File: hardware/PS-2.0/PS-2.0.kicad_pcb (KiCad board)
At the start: 2 copper layers, 119.7 x 199.4 mm, 51 parts, among them J1 PinSocket_02x16_P2.54mm_Verti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, J2 Conn_01x05, J3 Conn_01x05, J8 Conn_01x03, J9 Conn_01x03, K1 RAYEX-L90, K2 RAYEX-L90, Q1 IRFPE50, Q2 IRFPE50, Q3 IRFPE50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

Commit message: modified:   .DS_Store 	modified:   README.md 	deleted:    hardware/MSD-1.0/MSD-1.0 BoM.csv 	deleted:    hardware/MSD-1.0/MSD-1.0-backups/MSD-1.0-2025-04-08_110759.zip 	deleted:    hardware/MSD-1.0/MSD-1.0-backups/MSD-1.0-2025-04-08_111313.zip 	new file:   hardware/MSD-1.0/MSD-1.0-backups/MSD-1.0-2025-05-06_093009.zip 	new file:   hardware/MSD-1.0/MSD-1.0-backups/MSD-1.0-2025-05-06_093605.zip 	modified:   hardware/MSD-1.0/MSD-1.0.kicad_pcb 	modified:   hardware/MSD-1.0/MSD-1.0.kicad_sch 	modified:   hardware/MSD-1.0/fp-info-cache 	deleted:    hardware/PS-1.0/PS-1.0-backups/PS-1.0-2025-04-16_161300.zip 	deleted:    hardware/PS-1.0/PS-1.0-backups/PS-1.0-2025-04-16_162332.zip 	deleted:    hardware/PS-1.0/PS-1.0-backups/PS-1.0-2025-04-16_163259.zip 	deleted:    hardware/PS-1.0/PS-1.0-backups/PS-1.0-2025-04-17_110908.zip 	deleted:    hardware/PS-1.0/PS-1.0-backups/PS-1.0-2025-04-17_114838.zip 	deleted:    hardware/PS-1.0/PS-1.0-backups/PS-1.0-2025-04-17_155117.zip 	new file:   hardware/PS-1.0/PS-1.0-backups/PS-1.0-2025-05-06_094214.zip 	new file:   hardware/PS-1.0/PS-1.0-backups/PS-1.0-2025-05-06_095559.zip 	new file:   hardware/PS-1.0/PS-1.0-backups/PS-1.0-2025-05-06_100430.zip 	new file:   hardware/PS-1.0/PS-1.0-backups/PS-1.0-2025-05-06_100931.zip 	new file:   hardware/PS-1.0/PS-1.0-backups/PS-1.0-2025-05-06_101736.zip 	new file:   hardware/PS-1.0/PS-1.0-backups/PS-1.0-2025-05-06_102708.zip 	modified:   hardware/PS-1.0/PS-1.0.kicad_pcb 	modified:   hardware/PS-1.0/PS-1.0.kicad_sch 	new file:   hardware/PS-2.0/PS-2.0-B_Cu.gbr 	new file:   hardware/PS-2.0/PS-2.0-B_Mask.gbr 	new file:   hardware/PS-2.0/PS-2.0-B_Paste.gbr 	new file:   hardware/PS-2.0/PS-2.0-B_Silkscreen.gbr 	new file:   hardware/PS-2.0/PS-2.0-Edge_Cuts.gbr 	new file:   hardware/PS-2.0/PS-2.0-F_Cu.gbr 	new file:   hardware/PS-2.0/PS-2.0-F_Mask.gbr 	new file:   hardware/PS-2.0/PS-2.0-F_Paste.gbr 	new file:   hardware/PS-2.0/PS-2.0-F_Silkscreen.gbr 	new file:   hardware/PS-2.0/PS-2.0-NPTH.drl 	new file:   har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
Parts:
- moved D7 15.9 mm to (208.9, 196.8), turned to 0 degrees
- moved R5 13.3 mm to (229.2, 186.7), turned to 180 degrees
- moved L7 7.94 mm to (208.9, 191.8), turned to 0 degrees
- moved H1 5.72 mm to (216.2, 35.2)
- moved H2 5.72 mm to (216.2, 222.6)
- moved CON-01 3.51 mm to (232.9, 196.8)
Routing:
- net Net-(C4-Pad1): track 114.6 -> 186.0 mm
- net Net-(J1-Pin_9): track 85.7 -> 107.9 mm
- net Net-(J1-Pin_8): track 57.9 -> 77.3 mm
- net Net-(J1-Pin_7): track 61.7 -> 78.4 mm
- net Net-(J1-Pin_6): track 95.6 -> 110.5 mm
- net Net-(J1-Pin_5): track 98.4 -> 111.1 mm
- net /RLY-K: track 144.7 -> 155.2 mm
- net /RLY-A: track 124.0 -> 132.2 mm
- net /PWM: track 50.5 -> 54.7 mm
- added copper zone on B.Cu, net Net-(CON-01-Pin_2)
- added copper zone on B.Cu, net Net-(D7-K)
- added copper zone on B.Cu, net VS
- added copper zone on F.Cu, net VS

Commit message: modified:   .DS_Store 	modified:   README.md 	modified:   hardware/MSD-1.0/MSD-1.0-B_Cu.gbr 	modified:   hardware/MSD-1.0/MSD-1.0-B_Mask.gbr 	modified:   hardware/MSD-1.0/MSD-1.0-B_Paste.gbr 	modified:   hardware/MSD-1.0/MSD-1.0-B_Silkscreen.gbr 	modified:   hardware/MSD-1.0/MSD-1.0-Edge_Cuts.gbr 	modified:   hardware/MSD-1.0/MSD-1.0-F_Cu.gbr 	modified:   hardware/MSD-1.0/MSD-1.0-F_Mask.gbr 	modified:   hardware/MSD-1.0/MSD-1.0-F_Paste.gbr 	modified:   hardware/MSD-1.0/MSD-1.0-F_Silkscreen.gbr 	modified:   hardware/MSD-1.0/MSD-1.0-NPTH.drl 	modified:   hardware/MSD-1.0/MSD-1.0-PTH.drl 	deleted:    hardware/MSD-1.0/MSD-1.0-backups/MSD-1.0-2025-04-09_135836.zip 	deleted:    hardware/MSD-1.0/MSD-1.0-backups/MSD-1.0-2025-04-09_140350.zip 	new file:   hardware/MSD-1.0/MSD-1.0-backups/MSD-1.0-2025-05-08_171110.zip 	new file:   hardware/MSD-1.0/MSD-1.0-backups/MSD-1.0-2025-05-09_084805.zip 	modified:   hardware/MSD-1.0/MSD-1.0-job.gbrjob 	modified:   hardware/MSD-1.0/MSD-1.0.kicad_sch 	modified:   hardware/MSD-1.0/MSD-1.zip 	deleted:    hardware/MSD-1.0/~MSD-1.0.kicad_sch.lck 	modified:   hardware/PS-2.0/PS-2.0-B_Cu.gbr 	modified:   hardware/PS-2.0/PS-2.0-B_Mask.gbr 	modified:   hardware/PS-2.0/PS-2.0-B_Paste.gbr 	modified:   hardware/PS-2.0/PS-2.0-B_Silkscreen.gbr 	modified:   hardware/PS-2.0/PS-2.0-Edge_Cuts.gbr 	modified:   hardware/PS-2.0/PS-2.0-F_Cu.gbr 	modified:   hardware/PS-2.0/PS-2.0-F_Mask.gbr 	modified:   hardware/PS-2.0/PS-2.0-F_Paste.gbr 	modified:   hardware/PS-2.0/PS-2.0-F_Silkscreen.gbr 	modified:   hardware/PS-2.0/PS-2.0-NPTH.drl 	modified:   hardware/PS-2.0/PS-2.0-PTH.drl 	new file:   hardware/PS-2.0/PS-2.0-backups/PS-2.0-2025-05-09_084820.zip 	new file:   hardware/PS-2.0/PS-2.0-backups/PS-2.0-2025-05-09_090220.zip 	modified:   hardware/PS-2.0/PS-2.0-job.gbrjob 	modified:   hardware/PS-2.0/PS-2.0.kicad_pcb 	modified:   hardware/PS-2.0/PS-2.zip
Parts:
- removed HS3: Heatsink, Heatsink:Heatsink_Custom_10x18x50
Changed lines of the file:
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@@
 		)
 		(property "Value" "10A10"
-			(at 7.62 3.77 360)
+			(at 7.62 3.77 0)
 			(layer "F.Fab")
 			(effects
@@
 		)
 		(fp_text user "K"
-			(at 0 -2.3 360)
+			(at 0 -2.3 0)
 			(layer "F.Fab")
 			(effects
@@
 		)
 		(fp_text user "${REFERENCE}"
-			(at 8.295 0 360)
+			(at 8.295 0 0)
 			(layer "F.Fab")
 			(effects
@@
 		)
 		(property "Value" "L"
-			(at 7.62 3.12 360)
+			(at 7.62 3.12 0)
 			(layer "F.Fab")
 			(effects
@@
 		)
 		(fp_text user "${REFERENCE}"
-			(at 7.62 0 360)
+			(at 7.62 0 0)
 			(layer "F.Fab")
 			(effects
@@
 		)
 		(property "Value" "120Ω 2W"
-			(at 10.16 3.62 360)
+			(at 10.16 3.62 0)
 			(layer "F.Fab")
 			(effects
@@
 		)
 		(fp_text user "${REFERENCE}"
-			(at 10.16 0 360)
+			(at 10.16 0 0)
 			(layer "F.Fab")
 			(effects
@@
 			)
 			(scale
-				(xyz 1 1 1)
-			)
-			(rotate
-				(xyz 0 0 0)
-			)
-		)
-	)
-	(footprint "Heatsink:Heatsink_Custom_10x18x50"
-		(layer "F.Cu")
-		(at 230.8225 89.2175 -90)
-		(descr "Heatsink, StoneCold HS")
-		(tags "heatsink")
-		(property "Reference" "HS3"
-			(at 0 -8.85 90)
-			(layer "F.SilkS")
-			(hide yes)
-			(effects
-				(font
-					(size 1 1)
-					(thickness 0.15)
-				)
-			)
-		)
-		(property "Value" "Heatsink"
-			(at 0 -2.7 90)
-			(layer "F.Fab")
-			(hide yes)
-			(effects
-				(font
-					(size 1 1)
-					(thickness 0.15)
-				)
-			)
-		)
-		(property "Footprint" "Heatsink:Heatsink_Custom_10x18x50"
-			(at 0 -12.7 -90)
-			(unlocked yes)
-			(layer "F.Fab")
-			(hide yes)
-			(effects
-				(font
-					(size 1.27 1.27)
-					(thickness 0.15)
-				)
-			)
-		)
-		(property "Datasheet" ""
-			(at 0 -12.7 -90)
-			(unlocked yes)
-			(layer "F.Fab")
-			(hide yes)
-			(effects
-				(font
-					(size 1.27 1.27)
-					(thickness 0.15)
-				)
-			)
-		)
-		(property "Description" "Heatsink"
-			(at 0 -12.7 -90)
-			(unlocked yes)
-			(layer "F.Fab")
-			(hide yes)
-			(effects
-				(font
-					(size 1.27 1.27)
-					(thickness 0.15)
-				)
-			)
-		)
-		(property ki_fp_filters "Heatsink_*")
-		(sheetname "Root")
-		(sheetfile "PS-1.0.kicad_sch")
-		(attr through_hole)
-		(fp_line
-			(start -50 0)
-			(end -50 -18)
-			(stroke
-				(width 0.15)
-				(type default)
-			)
-			(layer "F.SilkS")
-		)
-		(fp_line
-			(start 50 0)
-			(end -50 0)
-			(stroke
-				(width 0.15)
-				(type default)
-			)
-			(layer "F.SilkS")
-		)
-		(fp_line
-			(start 50 0)
-			(end 50 -18)
-			(stroke
-				(width 0.15)
-				(type default)
-			)
-			(layer "F.SilkS")
-		)
-		(fp_line
-			(start 50 -18)
-			(end -50 -18)
-			(stroke
-				(width 0.15)
-				(type default)
-			)
-			(layer "F.SilkS")
-		)
-		(fp_line
-			(start -50 0)
-			(end -50 -18)
-			(stroke
-				(width 0.05)
-				(type default)
-			)
-			(layer "F.CrtYd")
-		)
-		(fp_line
-			(start 50 0)
-			(end -50 0)
-			(stroke
-				(width 0.05)
-				(type default)
-			)
-			(layer "F.CrtYd")
-		)
-		(fp_line
-			(start -50 -18)
-			(end 50 -18)
-			(stroke
-				(width 0.05)
-				(type default)
-			)
-			(layer "F.CrtYd")
-		)
-		(fp_line
-			(start 50 -18)
-			(end 50 0)
-			(stroke
-				(width 0.05)
-				(type default)
-			)
-			(layer "F.CrtYd")
-		)
-		(fp_text user "${REFERENCE}"
-			(at 0 -6.35 90)
-			(layer "F.Fab")
-			(effects
-				(font
-					(size 1 1)
-					(thickness 0.15)
-				)
-			)
-		)
-		(model "/Users/margabudi/Documents/ACAD/doc/Heatsink/10x18x50.step"
-			(offset
-				(xyz -50 0 0)
-			)
-			(scale

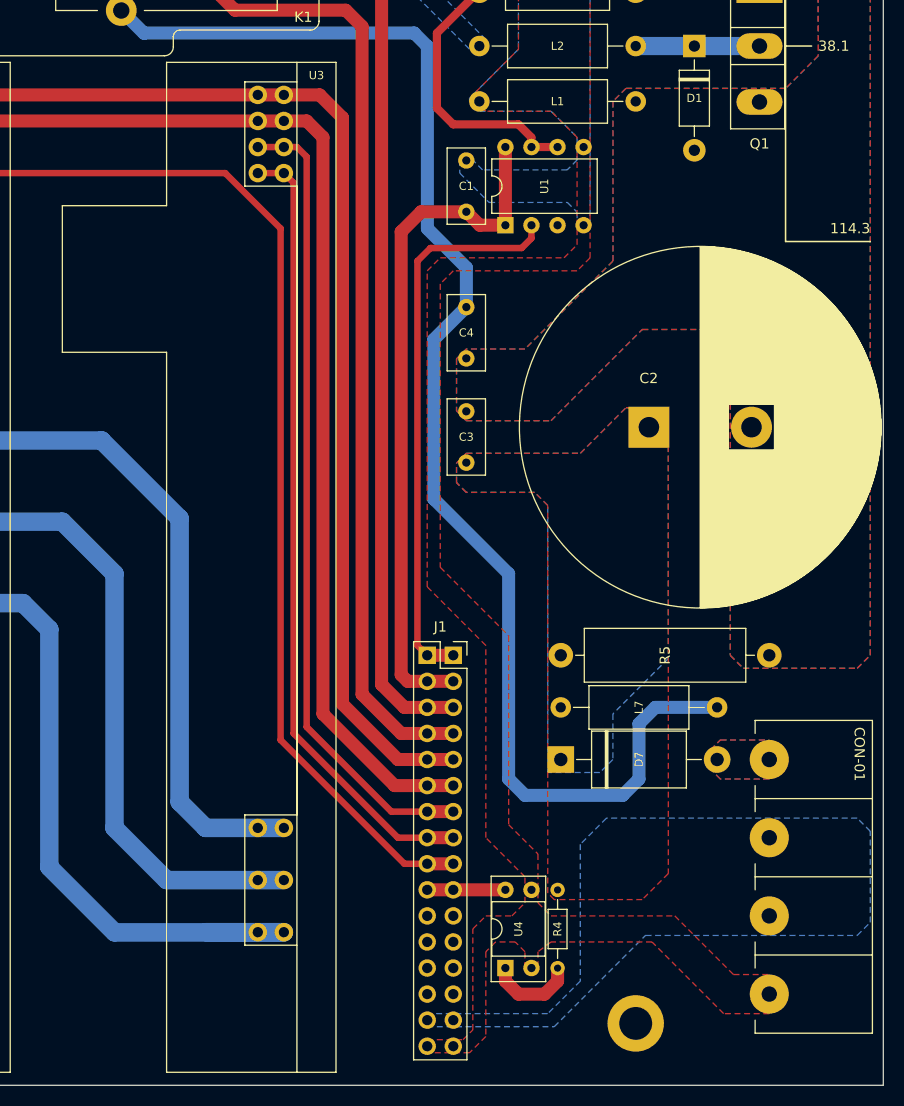
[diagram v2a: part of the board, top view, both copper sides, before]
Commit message: modified:   .DS_Store 	new file:   hardware/CTL-1.0/CTL-1.0-backups/CTL-1.0-2025-05-23_140814.zip 	new file:   hardware/CTL-1.0/CTL-1.0-backups/CTL-1.0-2025-05-23_142136.zip 	new file:   hardware/CTL-1.0/CTL-1.0-backups/CTL-1.0-2025-05-23_145207.zip 	new file:   hardware/CTL-1.0/CTL-1.0-backups/CTL-1.0-2025-05-23_145749.zip 	new file:   hardware/CTL-1.0/CTL-1.0-backups/CTL-1.0-2025-05-27_175205.zip 	new file:   hardware/CTL-1.0/CTL-1.0-backups/CTL-1.0-2025-05-27_180035.zip 	new file:   hardware/CTL-1.0/CTL-1.0-backups/CTL-1.0-2025-05-27_181441.zip 	new file:   hardware/CTL-1.0/CTL-1.0-backups/CTL-1.0-2025-05-27_182529.zip 	new file:   hardware/CTL-1.0/CTL-1.0-backups/CTL-1.0-2025-05-27_183819.zip 	new file:   hardware/CTL-1.0/CTL-1.0-backups/CTL-1.0-2025-05-28_201558.zip 	new file:   hardware/CTL-1.0/CTL-1.0-backups/CTL-1.0-2025-05-28_202523.zip 	new file:   hardware/CTL-1.0/CTL-1.0-backups/CTL-1.0-2025-05-28_203223.zip 	new file:   hardware/CTL-1.0/CTL-1.0-backups/CTL-1.0-2025-05-28_203806.zip 	new file:   hardware/CTL-1.0/CTL-1.0-backups/CTL-1.0-2025-05-28_204313.zip 	new file:   hardware/CTL-1.0/CTL-1.0-backups/CTL-1.0-2025-05-30_173028.zip 	new file:   hardware/CTL-1.0/CTL-1.0-backups/CTL-1.0-2025-05-30_174116.zip 	new file:   hardware/CTL-1.0/CTL-1.0-backups/CTL-1.0-2025-05-30_175122.zip 	new file:   hardware/CTL-1.0/CTL-1.0-backups/CTL-1.0-2025-05-30_180325.zip 	new file:   hardware/CTL-1.0/CTL-1.0-backups/CTL-1.0-2025-05-30_180909.zip 	new file:   hardware/CTL-1.0/CTL-1.0-backups/CTL-1.0-2025-06-03_185115.zip 	new file:   hardware/CTL-1.0/CTL-1.0-backups/CTL-1.0-2025-06-03_190157.zip 	new file:   hardware/CTL-1.0/CTL-1.0-backups/CTL-1.0-2025-06-03_222127.zip 	new file:   hardware/CTL-1.0/CTL-1.0-backups/CTL-1.0-2025-06-03_222647.zip 	new file:   hardware/CTL-1.0/CTL-1.0-backups/CTL-1.0-2025-06-03_223358.zip 	new file:   hardware/CTL-1.0/CTL-1.0-backups/CTL-1.0-2025-06-03_223905.zip 	modified:   hardware/CTL-1.0/CTL-1.0.kicad_pcb 	new file:   hardware/CTL-1.0/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
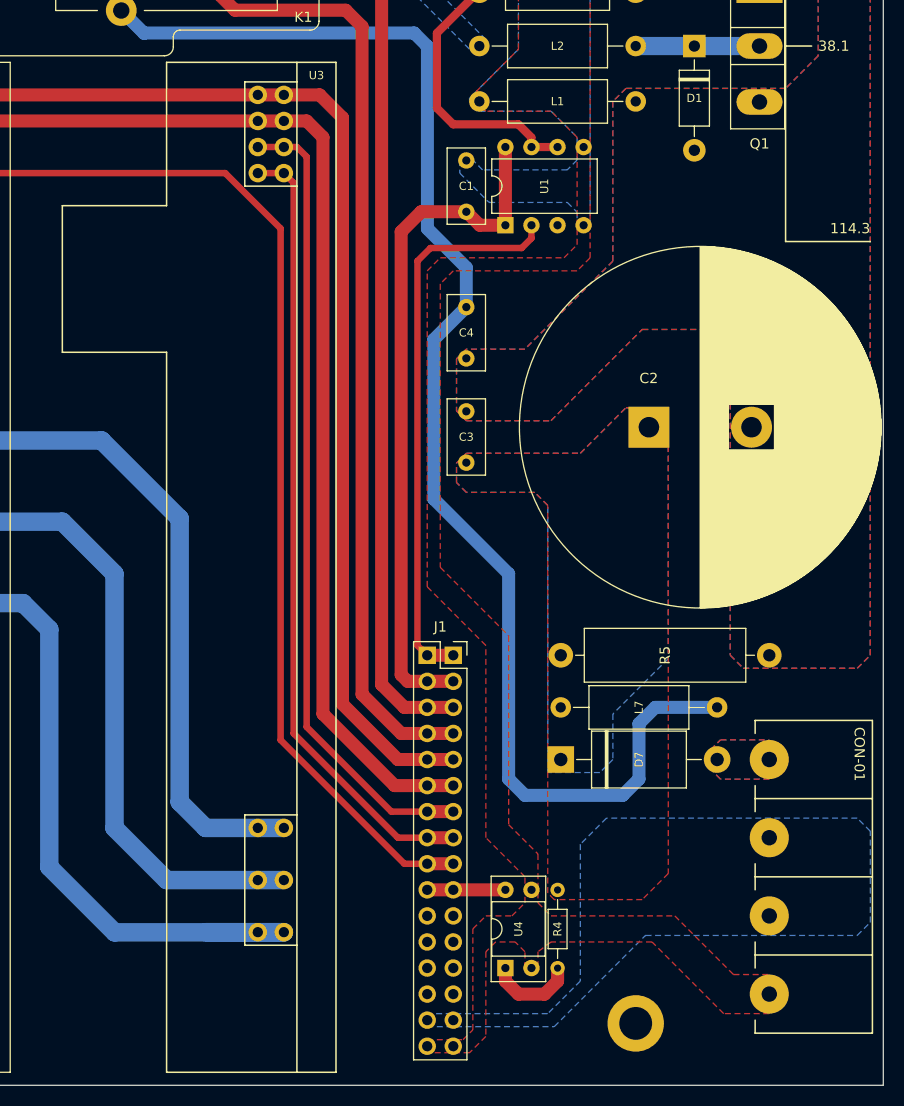
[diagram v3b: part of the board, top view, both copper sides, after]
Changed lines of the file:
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@@
 			(end -22.86 28.2575)
 			(stroke
-				(width 0.1)
+				(width 0.15)
 				(type default)
 			)
@@
 			(end -12.7 28.2575)
 			(stroke
-				(width 0.1)
+				(width 0.15)
 				(type default)
 			)
@@
 			(end -12.7 13.97)
 			(stroke
-				(width 0.1)
+				(width 0.15)
 				(type default)
 			)
@@
 			(end -22.86 13.97)
 			(stroke
-				(width 0.1)
+				(width 0.15)
 				(type default)
 			)
@@
 			(end -12.7 98.425)
 			(stroke
-				(width 0.1)
+				(width 0.15)
 				(type default)
 			)
@@
 			(end -5.08 12.065)
 			(stroke
-				(width 0.1)
+				(width 0.15)
 				(type default)
 			)
@@
 			(end 0 12.065)
 			(stroke
-				(width 0.1)
+				(width 0.15)
 				(type default)
 			)
@@
 			(end -5.08 86.0425)
 			(stroke
-				(width 0.1)
+				(width 0.15)
 				(type default)
 			)
@@
 			(end 0 86.0425)
 			(stroke
-				(width 0.1)
+				(width 0.15)
 				(type default)
 			)
@@
 			(end 0 98.425)
 			(stroke
-				(width 0.1)
+				(width 0.15)
 				(type default)
 			)
@@
 			(end -5.08 1.905)
 			(stroke
-				(width 0.1)
-				(type default)
-			)
-			(layer "F.SilkS")
-		)
-		(fp_line
-			(start 0 12.065)
-			(end 0 73.3425)
-			(stroke
-				(width 0.1)
+				(width 0.15)
 				(type default)
 			)
@@
 			(end -5.08 73.3425)
 			(stroke
-				(width 0.1)
+				(width 0.15)
 				(type default)
 			)
@@
 			(end -12.7 0)
 			(stroke
-				(width 0.1)
+				(width 0.15)
 				(type default)
 			)
@@
 			(end 3.81 98.425)
 			(stroke
-				(width 0.1)
+				(width 0.15)
 				(type default)
 			)
@@
 			(end -12.7 98.425)
 			(stroke
-				(width 0.1)
+				(width 0.15)
 				(type default)
 			)
@@
 			(end -2.54 5.08)
 			(stroke
-				(width 0.1)
+				(width 0.15)
 				(type default)
 			)
@@
 			(end 5.08 5.08)
 			(stroke
-				(width 0.1)
+				(width 0.15)
 				(type default)
 			)
@@
 			(end 3.81 -6.35)
 			(stroke
-				(width 0.1)
+				(width 0.15)
 				(type default)
 			)
@@
 			(end 12.7 5.08)
 			(stroke
-				(width 0.1)
+				(width 0.15)
 				(type default)
 			)
@@
 			(end 11.43 -6.35)
 			(stroke
-				(width 0.1)
+				(width 0.15)
 				(type default)
 			)
@@
 			(end 20.32 5.08)
 			(stroke
-				(width 0.1)
+				(width 0.15)
 				(type default)
 			)
@@
 			(end 19.05 -6.35)
 			(stroke
-				(width 0.1)
+				(width 0.15)
 				(type default)
 			)
@@
 			(end 26.67 5.08)
 			(stroke
-				(width 0.1)
+				(width 0.15)
 				(type default)
 			)
@@
 			(end -3.81 5.08)
 			(stroke
-				(width 0.1)
+				(width 0.15)
 				(type default)
 			)
@@
 			(end 26.67 -6.35)
 			(stroke
-				(width 0.1)
+				(width 0.15)
 				(type default)
 			)
@@
 			(end 26.67 5.08)
 			(stroke
-				(width 0.1)
-				(type default)
-			)
+				(width 0.15)
+				(type default)
+			)
